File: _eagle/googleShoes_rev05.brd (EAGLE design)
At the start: 87.6 x 38.1 mm, 54 parts, among them Q1 MMBT2222A, U1 MCP73831, U2 3.3V, U3 ATMEGA328, U4 TPA2005D1DRB, Y1 8MHz

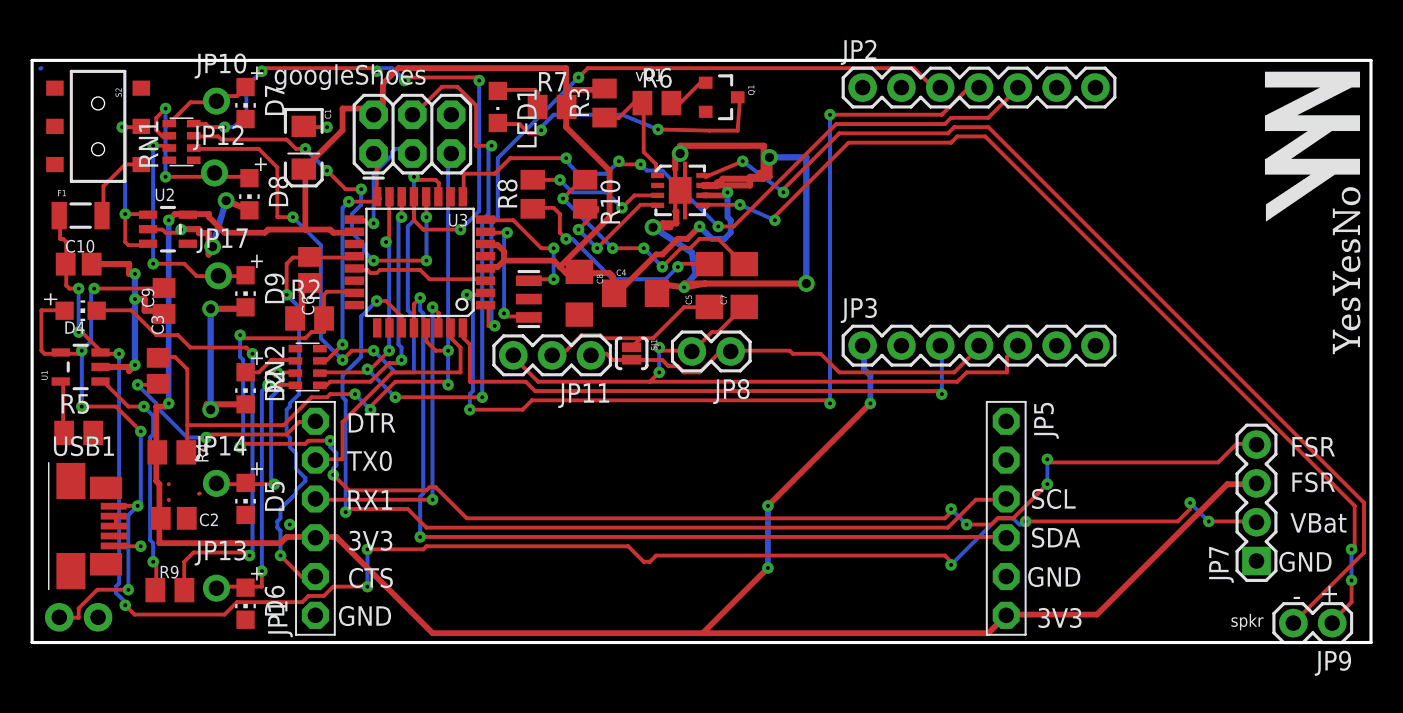
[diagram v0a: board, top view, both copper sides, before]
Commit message: updated vbatt line, drill sizes
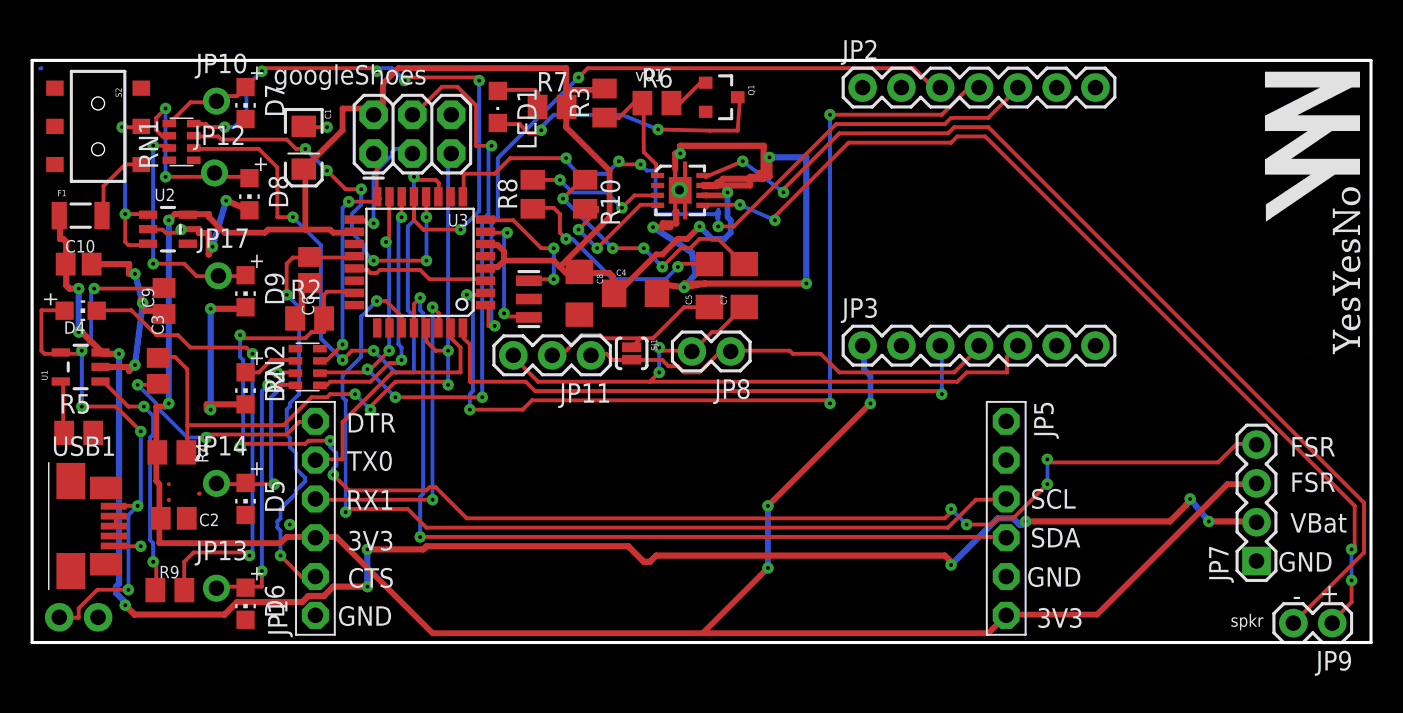
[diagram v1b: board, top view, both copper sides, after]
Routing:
- net D5: track 44.6 -> 48.4 mm
- net GND: track 106.2 -> 106.0 mm, vias 15 -> 16

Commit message: fixed ERC errors
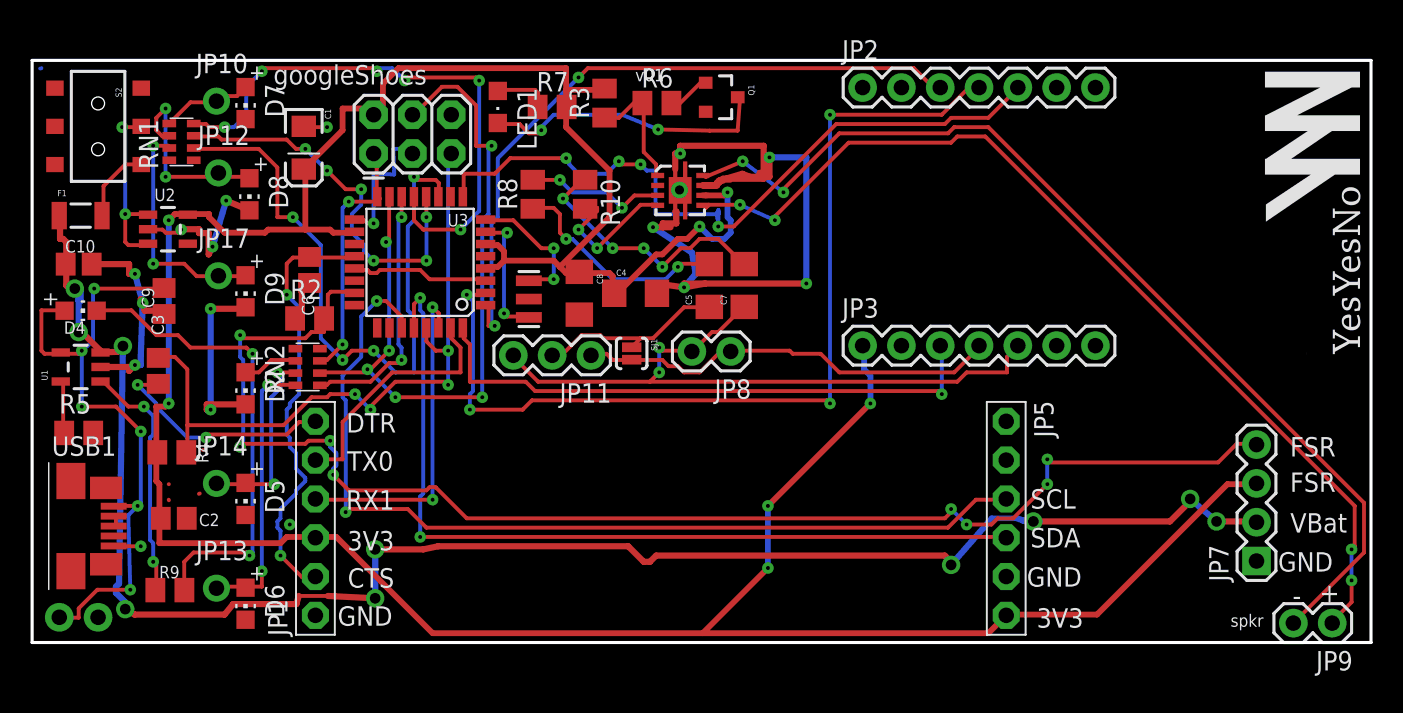
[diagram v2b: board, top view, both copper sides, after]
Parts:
- moved JP12 0.25 mm to (12.2, 30.7)
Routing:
- net VBATT: track 110.1 -> 113.2 mm
- net GND: track 106.0 -> 107.4 mm, vias 16 -> 17
- net SCK: track 8.07 -> 9.01 mm
